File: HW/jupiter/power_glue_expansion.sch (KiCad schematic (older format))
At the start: 22 parts

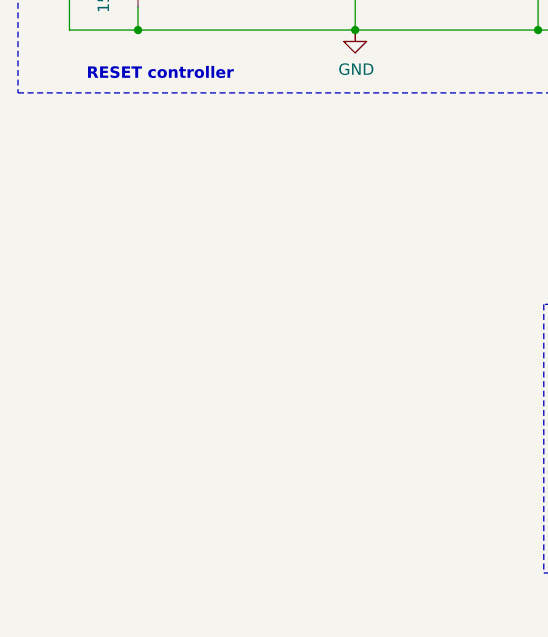
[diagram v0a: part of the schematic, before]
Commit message: Schematics to clock, reset, panic and power section done.
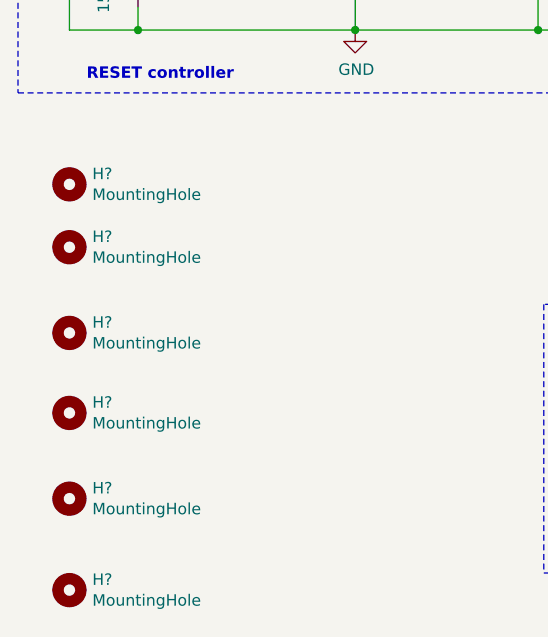
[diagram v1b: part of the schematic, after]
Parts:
- added H? (x6): MountingHole, symbol Mechanical:MountingHole
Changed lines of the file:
@@
 encoding utf-8
 Sheet 2 2
-Title "Glue, control logic and expansion"
+Title "Glue and power supply"
 Date "2019-06-23"
 Rev "0.1"
@@
 Wire Notes Line
 	6450 3850 6450 1775
+$Comp
+L Mechanical:MountingHole H?
+U 1 1 5D2A33B9
+P 975 4350
+F 0 "H?" H 1075 4396 50  0000 L CNN
+F 1 "MountingHole" H 1075 4305 50  0000 L CNN
+F 2 "" H 975 4350 50  0001 C CNN
+F 3 "~" H 975 4350 50  0001 C CNN
+	1    975  4350
+	1    0    0    -1
+$EndComp
+$Comp
+L Mechanical:MountingHole H?
+U 1 1 5D2A481F
+P 975 4625
+F 0 "H?" H 1075 4671 50  0000 L CNN
+F 1 "MountingHole" H 1075 4580 50  0000 L CNN
+F 2 "" H 975 4625 50  0001 C CNN
+F 3 "~" H 975 4625 50  0001 C CNN
+	1    975  4625
+	1    0    0    -1
+$EndComp
+$Comp
+L Mechanical:MountingHole H?
+U 1 1 5D2A4D03
+P 975 5000
+F 0 "H?" H 1075 5046 50  0000 L CNN
+F 1 "MountingHole" H 1075 4955 50  0000 L CNN
+F 2 "" H 975 5000 50  0001 C CNN
+F 3 "~" H 975 5000 50  0001 C CNN
+	1    975  5000
+	1    0    0    -1
+$EndComp
+$Comp
+L Mechanical:MountingHole H?
+U 1 1 5D2A515B
+P 975 5350
+F 0 "H?" H 1075 5396 50  0000 L CNN
+F 1 "MountingHole" H 1075 5305 50  0000 L CNN
+F 2 "" H 975 5350 50  0001 C CNN
+F 3 "~" H 975 5350 50  0001 C CNN
+	1    975  5350
+	1    0    0    -1
+$EndComp
+$Comp
+L Mechanical:MountingHole H?
+U 1 1 5D2A562D
+P 975 5725
+F 0 "H?" H 1075 5771 50  0000 L CNN
+F 1 "MountingHole" H 1075 5680 50  0000 L CNN
+F 2 "" H 975 5725 50  0001 C CNN
+F 3 "~" H 975 5725 50  0001 C CNN
+	1    975  5725
+	1    0    0    -1
+$EndComp
+$Comp
+L Mechanical:MountingHole H?
+U 1 1 5D2A5A6E
+P 975 6125
+F 0 "H?" H 1075 6171 50  0000 L CNN
+F 1 "MountingHole" H 1075 6080 50  0000 L CNN
+F 2 "" H 975 6125 50  0001 C CNN
+F 3 "~" H 975 6125 50  0001 C CNN
+	1    975  6125
+	1    0    0    -1
+$EndComp
 $EndSCHEMATC
